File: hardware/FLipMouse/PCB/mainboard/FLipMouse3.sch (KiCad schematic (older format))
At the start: 90 parts, among them J1 SJ2-3574A, J2 SJ2-3574A, J3 M50-3900542, J4 Conn_ARM_JTAG_SWD_10, J5 Conn_02x05_Odd_Even, J6 USB_OTG, J7 Conn_01x06, Q1 BC847, Q2 BC847, Q3 BSH108, Q4 BSH108, Q5 Si2301, SW1 SW_Push, SW2 SW_Push, U1 ESP32-WROOM, U2 TSOP4838, U3 LPC11U24FBD, U4 TSR_1-2433, U5 MPXV7007GP, U6 AP2127N-3.3, Y1 JA-12.000-18-DFE

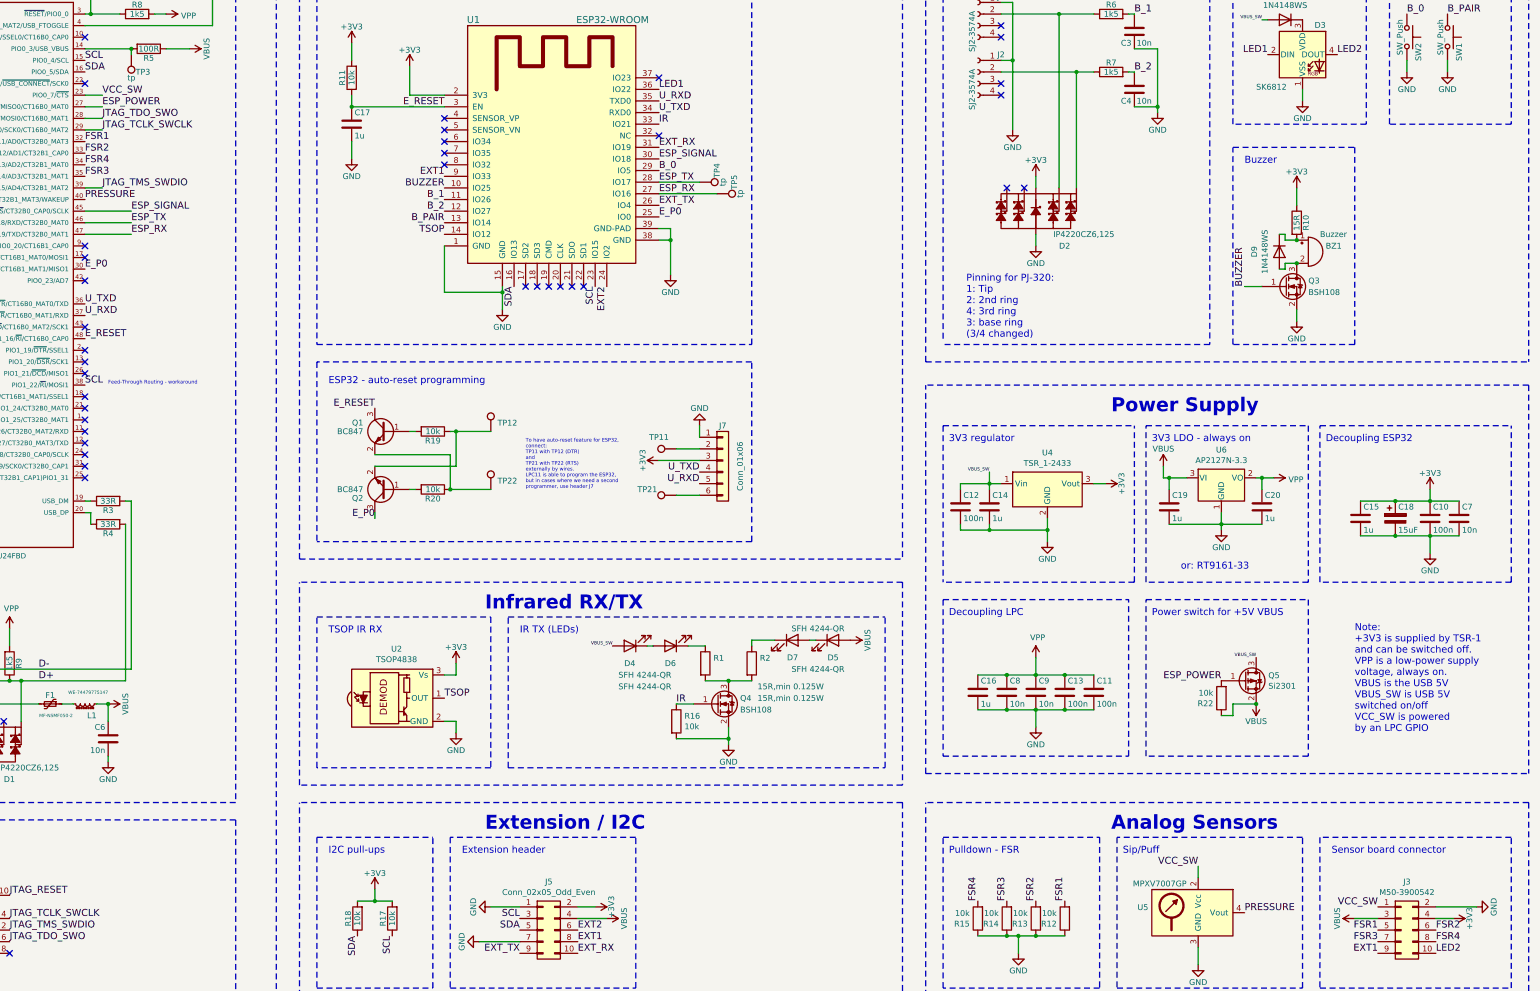
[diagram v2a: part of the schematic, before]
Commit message: Unified 3V3 (switched), according to chapter 9.4 of LPC datasheet, the high power pin doesn't deliver 3v3.
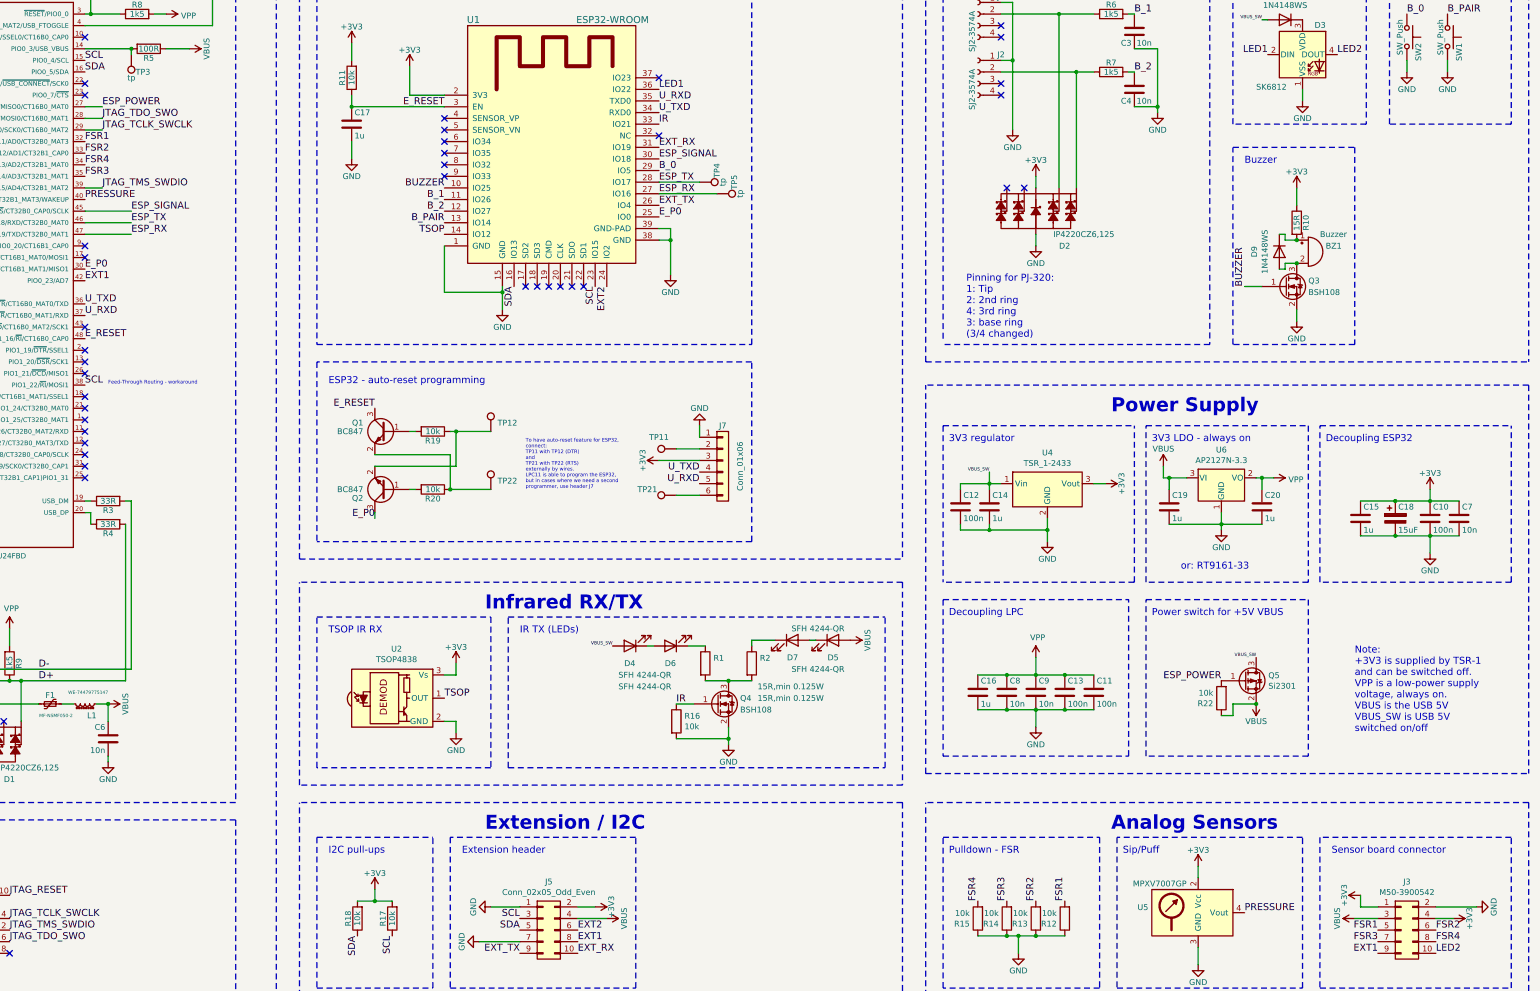
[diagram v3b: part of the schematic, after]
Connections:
- net +3V3: now also J3.1 (Pin_1), U5.2 (Vcc)
- net EXT1: now also U3.42 (PIO0_23/AD7); no longer U1.9 (IO33)
- removed net VCC_SW: J3.1 (Pin_1), U3.23 (PIO0_7/~CTS~), U5.2 (Vcc)
- no-connect marks 39 -> 40
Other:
- note added: "Note:\n+3V3 is supplied by TSR-1 \nand can be switched off.\nVPP is a low-power supply \nvoltage, always on.\nVBUS is the USB 5V\nVBUS_SW is USB 5V\nswitched on/off"
- note removed: "Note:\n+3V3 is supplied by TSR-1 \nand can be switched off.\nVPP is a low-power supply \nvoltage, always on.\nVBUS is the USB 5V\nVBUS_SW is USB 5V\nswitched on/off\nVCC_SW is powered\nby an LPC GPIO"
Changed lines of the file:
@@
 NoConn ~ 3500 5200
 NoConn ~ 3500 3300
-NoConn ~ 3500 3600
 NoConn ~ 3500 4300
 NoConn ~ 3500 4400
@@
 Text Label 15150 9300 0    60   ~ 0
 FSR4
-Text Label 6600 2700 2    60   ~ 0
+Text Label 3500 3600 0    60   ~ 0
 EXT1
 Text Label 5850 9250 3    60   ~ 0
@@
 Text Notes 10950 8550 0    60   ~ 0
 Pulldown - FSR
-Wire Wire Line
-	13100 8650 13100 8750
 Wire Wire Line
 	13100 9500 13100 9350
@@
 $EndComp
 Text Notes 14450 7500 0    60   ~ 0
-Note:\n+3V3 is supplied by TSR-1 \nand can be switched off.\nVPP is a low-power supply \nvoltage, always on.\nVBUS is the USB 5V\nVBUS_SW is USB 5V\nswitched on/off\nVCC_SW is powered\nby an LPC GPIO
+Note:\n+3V3 is supplied by TSR-1 \nand can be switched off.\nVPP is a low-power supply \nvoltage, always on.\nVBUS is the USB 5V\nVBUS_SW is USB 5V\nswitched on/off
 $Comp
 L power:GND #PWR033
@@
 	13300 5700 13650 5700
 Wire Wire Line
-	3500 2000 3650 2000
-Text Label 3650 2000 0    60   ~ 0
-VCC_SW
-Wire Wire Line
 	15500 9000 15150 9000
-Text Label 14650 9000 2    60   ~ 0
-VCC_SW
 $Comp
 L power:+3V3 #PWR042
@@
 	1    0    0    -1
 $EndComp
-Text Label 13100 8650 2    60   ~ 0
-VCC_SW
 $Comp
 L Device:D D9
@@
 	13850 3450 13950 3450
 Connection ~ 13950 3450
+$Comp
+L power:+3V3 #PWR0101
+U 1 1 5C9F4727
+P 14500 8900
+F 0 "#PWR0101" H 14500 8750 50  0001 C CNN
+F 1 "+3V3" H 14500 9040 50  0000 C CNN
+F 2 "" H 14500 8900 50  0001 C CNN
+F 3 "" H 14500 8900 50  0001 C CNN
+	1    14500 8900
+	0    -1   -1   0
+$EndComp
+Wire Wire Line
+	14500 8900 14500 9000
+Wire Wire Line
+	14500 9000 14650 9000
+NoConn ~ 6600 2700
+$Comp
+L power:+3V3 #PWR0102
+U 1 1 5CA15D15
+P 13100 8650
+F 0 "#PWR0102" H 13100 8500 50  0001 C CNN
+F 1 "+3V3" H 13100 8790 50  0000 C CNN
+F 2 "" H 13100 8650 50  0001 C CNN
+F 3 "" H 13100 8650 50  0001 C CNN
+	1    13100 8650
+	1    0    0    -1
+$EndComp
+Wire Wire Line
+	13100 8650 13100 8750
+NoConn ~ 3500 2000
 $EndSCHEMATC
